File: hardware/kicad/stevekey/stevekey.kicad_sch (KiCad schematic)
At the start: 23 parts, among them J1 ATMEL-ICE-10, J2 Conn_01x04, J3 Conn_01x02, J4 Conn_01x02, J5 Conn_01x02, Q1 2N3904, SW1 SW_SL, SW2 SW_CAPS, SW3 SW_4080, U1 CD4066BM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

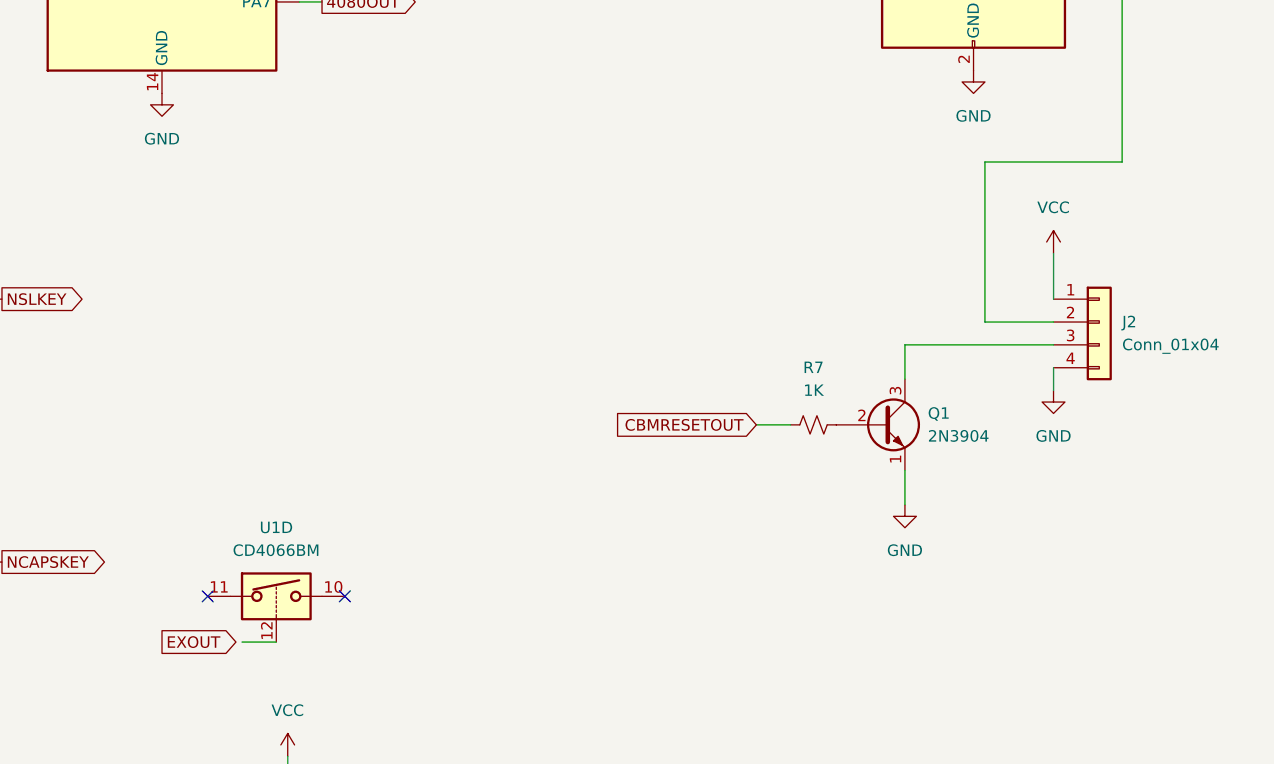
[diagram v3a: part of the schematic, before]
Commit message: Bring the extra 4066 pins out to the header
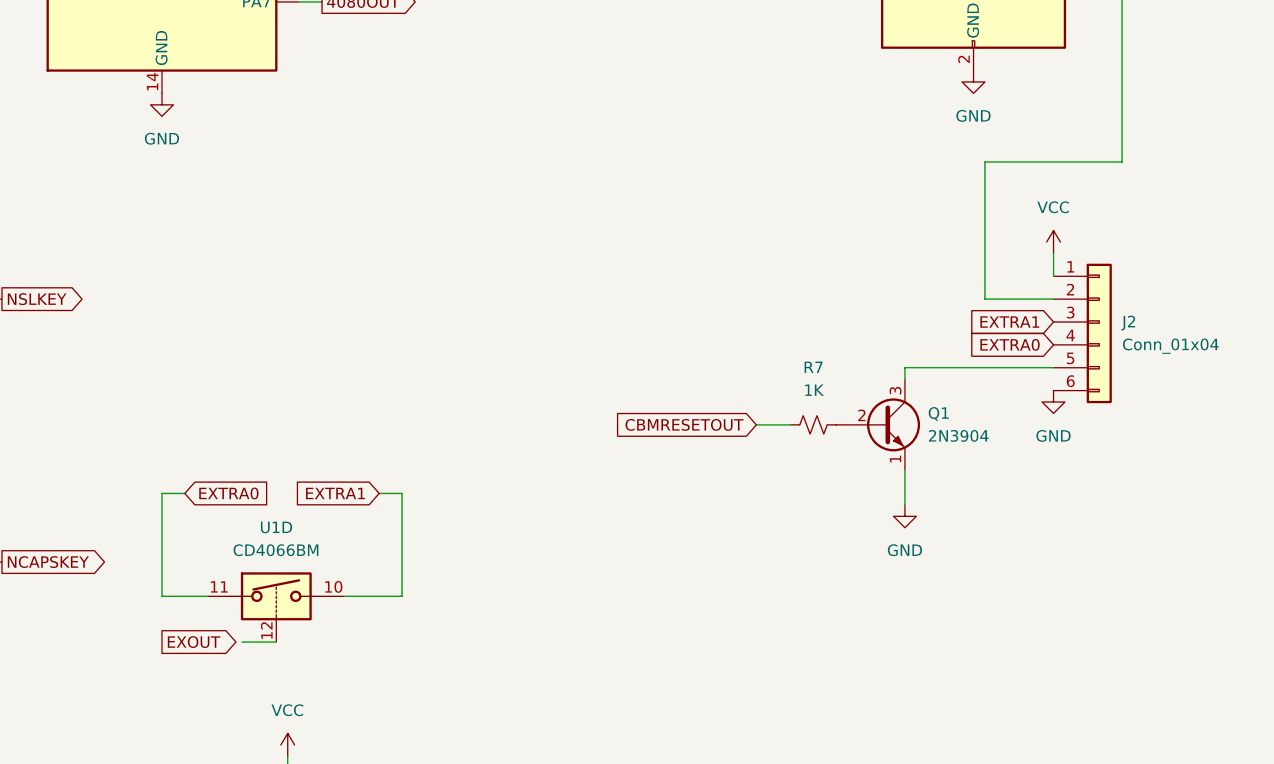
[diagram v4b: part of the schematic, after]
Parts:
- J2: footprint Connector_PinHeader_2.54mm:PinHeader_1x04_P2.54mm_Vertical -> Connector_PinHeader_2.54mm:PinHeader_1x06_P2.54mm_Vertical; symbol Connector_Generic:Conn_01x04 -> Connector_Generic:Conn_01x06
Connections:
- net GND: now also J2.6 (Pin_6); no longer J2.4 (Pin_4)
- net at Q1.3 (C): now also J2.5 (Pin_5); no longer J2.3 (Pin_3)
- net EXTRA1: now reaches U1.10
- net EXTRA1: now also J2.3 (Pin_3)
- net EXTRA0: now reaches U1.11
- net EXTRA0: now also J2.4 (Pin_4)
- no-connect marks 7 -> 5
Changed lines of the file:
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@@
   )
   (no_connect (at 186.69 71.12))
-  (no_connect (at 104.14 147.32))
   (no_connect (at 186.69 66.04))
   (no_connect (at 186.69 73.66))
-  (no_connect (at 88.9 147.32))
   (no_connect (at 186.69 68.58))
   (no_connect (at 186.69 78.74))
@@
     (stroke (width 0) (type default))
   )
+  (wire (pts (xy 107.95 135.89) (xy 110.49 135.89))
+    (stroke (width 0) (type default))
+  )
   (wire (pts (xy 190.5 76.2) (xy 190.5 99.06))
     (stroke (width 0) (type default))
   )
+  (wire (pts (xy 110.49 135.89) (xy 110.49 147.32))
+    (stroke (width 0) (type default))
+  )
   (wire (pts (xy 33.02 116.84) (xy 33.02 105.41))
     (stroke (width 0) (type default))
@@
     (stroke (width 0) (type default))
   )
-  (wire (pts (xy 182.88 121.92) (xy 182.88 124.46))
-    (stroke (width 0) (type default))
-  )
   (wire (pts (xy 40.64 66.04) (xy 53.34 66.04))
     (stroke (width 0) (type default))
@@
     (stroke (width 0) (type default))
   )
+  (wire (pts (xy 182.88 109.22) (xy 182.88 111.76))
+    (stroke (width 0) (type default))
+  )
   (wire (pts (xy 43.18 58.42) (xy 43.18 63.5))
     (stroke (width 0) (type default))
@@
     (stroke (width 0) (type default))
   )
+  (wire (pts (xy 83.82 147.32) (xy 88.9 147.32))
+    (stroke (width 0) (type default))
+  )
   (wire (pts (xy 115.57 55.88) (xy 115.57 58.42))
     (stroke (width 0) (type default))
   )
+  (wire (pts (xy 110.49 147.32) (xy 104.14 147.32))
+    (stroke (width 0) (type default))
+  )
+  (wire (pts (xy 166.37 121.92) (xy 166.37 123.19))
+    (stroke (width 0) (type default))
+  )
   (wire (pts (xy 100.33 59.69) (xy 100.33 63.5))
     (stroke (width 0) (type default))
@@
     (stroke (width 0) (type default))
   )
-  (wire (pts (xy 182.88 109.22) (xy 182.88 114.3))
-    (stroke (width 0) (type default))
-  )
   (wire (pts (xy 53.34 45.72) (xy 53.34 53.34))
     (stroke (width 0) (type default))
@@
     (stroke (width 0) (type default))
   )
-  (wire (pts (xy 175.26 116.84) (xy 175.26 99.06))
+  (wire (pts (xy 175.26 99.06) (xy 175.26 114.3))
     (stroke (width 0) (type default))
   )
@@
     (stroke (width 0) (type default))
   )
-  (wire (pts (xy 182.88 116.84) (xy 175.26 116.84))
-    (stroke (width 0) (type default))
-  )
   (wire (pts (xy 186.69 76.2) (xy 190.5 76.2))
     (stroke (width 0) (type default))
@@
     (stroke (width 0) (type default))
   )
-  (wire (pts (xy 182.88 119.38) (xy 166.37 119.38))
-    (stroke (width 0) (type default))
-  )
   (wire (pts (xy 33.02 167.64) (xy 33.02 179.07))
     (stroke (width 0) (type default))
@@
     (stroke (width 0) (type default))
   )
-  (wire (pts (xy 166.37 119.38) (xy 166.37 123.19))
-    (stroke (width 0) (type default))
-  )
   (wire (pts (xy 99.06 76.2) (xy 101.6 76.2))
     (stroke (width 0) (type default))
@@
     (stroke (width 0) (type default))
   )
+  (wire (pts (xy 83.82 135.89) (xy 83.82 147.32))
+    (stroke (width 0) (type default))
+  )
   (wire (pts (xy 135.89 45.72) (xy 135.89 50.8))
     (stroke (width 0) (type default))
   )
+  (wire (pts (xy 86.36 135.89) (xy 83.82 135.89))
+    (stroke (width 0) (type default))
+  )
   (wire (pts (xy 55.88 114.3) (xy 55.88 118.11))
     (stroke (width 0) (type default))
@@
     (stroke (width 0) (type default))
   )
+  (wire (pts (xy 166.37 121.92) (xy 182.88 121.92))
+    (stroke (width 0) (type default))
+  )
   (wire (pts (xy 99.06 81.28) (xy 101.6 81.28))
     (stroke (width 0) (type default))
@@
     (stroke (width 0) (type default))
   )
+  (wire (pts (xy 182.88 114.3) (xy 175.26 114.3))
+    (stroke (width 0) (type default))
+  )
   (image (at 245.11 80.01) (scale 1.04059)
     (data
@@
     )
   )
+  (global_label "EXTRA1" (shape input) (at 107.95 135.89 180) (fields_autoplaced)
+    (effects (font (size 1.27 1.27)) (justify right))
+    (property "Intersheetrefs" "${INTERSHEET_REFS}" (at 98.0706 135.89 0)
+      (effects (font (size 1.27 1.27)) (justify right) hide)
+    )
+  )
   (global_label "NSLKEY" (shape output) (at 66.04 114.3 0) (fields_autoplaced)
     (effects (font (size 1.27 1.27)) (justify left))
@@
     )
   )
+  (global_label "EXTRA1" (shape input) (at 182.88 116.84 180) (fields_autoplaced)
+    (effects (font (size 1.27 1.27)) (justify right))
+    (property "Intersheetrefs" "${INTERSHEET_REFS}" (at 173.0006 116.84 0)
+      (effects (font (size 1.27 1.27)) (justify right) hide)
+    )
+  )
   (global_label "4080OUT" (shape input) (at 35.56 186.69 180) (fields_autoplaced)
     (effects (font (size 1.27 1.27)) (justify right))
@@
     )
   )
+  (global_label "EXTRA0" (shape input) (at 182.88 119.38 180) (fields_autoplaced)
+    (effects (font (size 1.27 1.27)) (justify right))
+    (property "Intersheetrefs" "${INTERSHEET_REFS}" (at 173.0006 119.38 0)
+      (effects (font (size 1.27 1.27)) (justify right) hide)
+    )
+  )
   (global_label "EXOUT" (shape output) (at 101.6 73.66 0) (fields_autoplaced)
     (effects (font (size 1.27 1.27)) (justify left))
@@
     )
   )
+  (global_label "EXTRA0" (shape input) (at 86.36 135.89 0) (fields_autoplaced)
+    (effects (font (size 1.27 1.27)) (justify left))
+    (property "Intersheetrefs" "${INTERSHEET_REFS}" (at 96.2394 135.89 0)
+      (effects (font (size 1.27 1.27)) (justify left) hide)
+    )
+  )
   (global_label "CBMRESETOUT" (shape input) (at 149.86 128.27 180) (fields_autoplaced)
     (effects (font (size 1.27 1.27)) (justify right))
@@
     )
   )
-  (symbol (lib_id "Connector_Generic:Conn_01x04") (at 187.96 116.84 0) (unit 1)
+  (symbol (lib_id "Connector_Generic:Conn_01x06") (at 187.96 116.84 0) (unit 1)
     (in_bom yes) (on_board yes) (dnp no) (fields_autoplaced)
     (property "Reference" "J2" (at 190.5 116.84 0)
@@
       (effects (font (size 1.27 1.27)) (justify left))
     )
-    (property "Footprint" "Connector_PinHeader_2.54mm:PinHeader_1x04_P2.54mm_Vertical" (at 187.96 116.84 0)
+    (property "Footprint" "Connector_PinHeader_2.54mm:PinHeader_1x06_P2.54mm_Vertical" (at 187.96 116.84 0)
       (effects (font (size 1.27 1.27)) hide)
     )
@@
     (pin "3")
     (pin "4")
+    (pin "5")
+    (pin "6")
     (instances
       (project "stevekey"

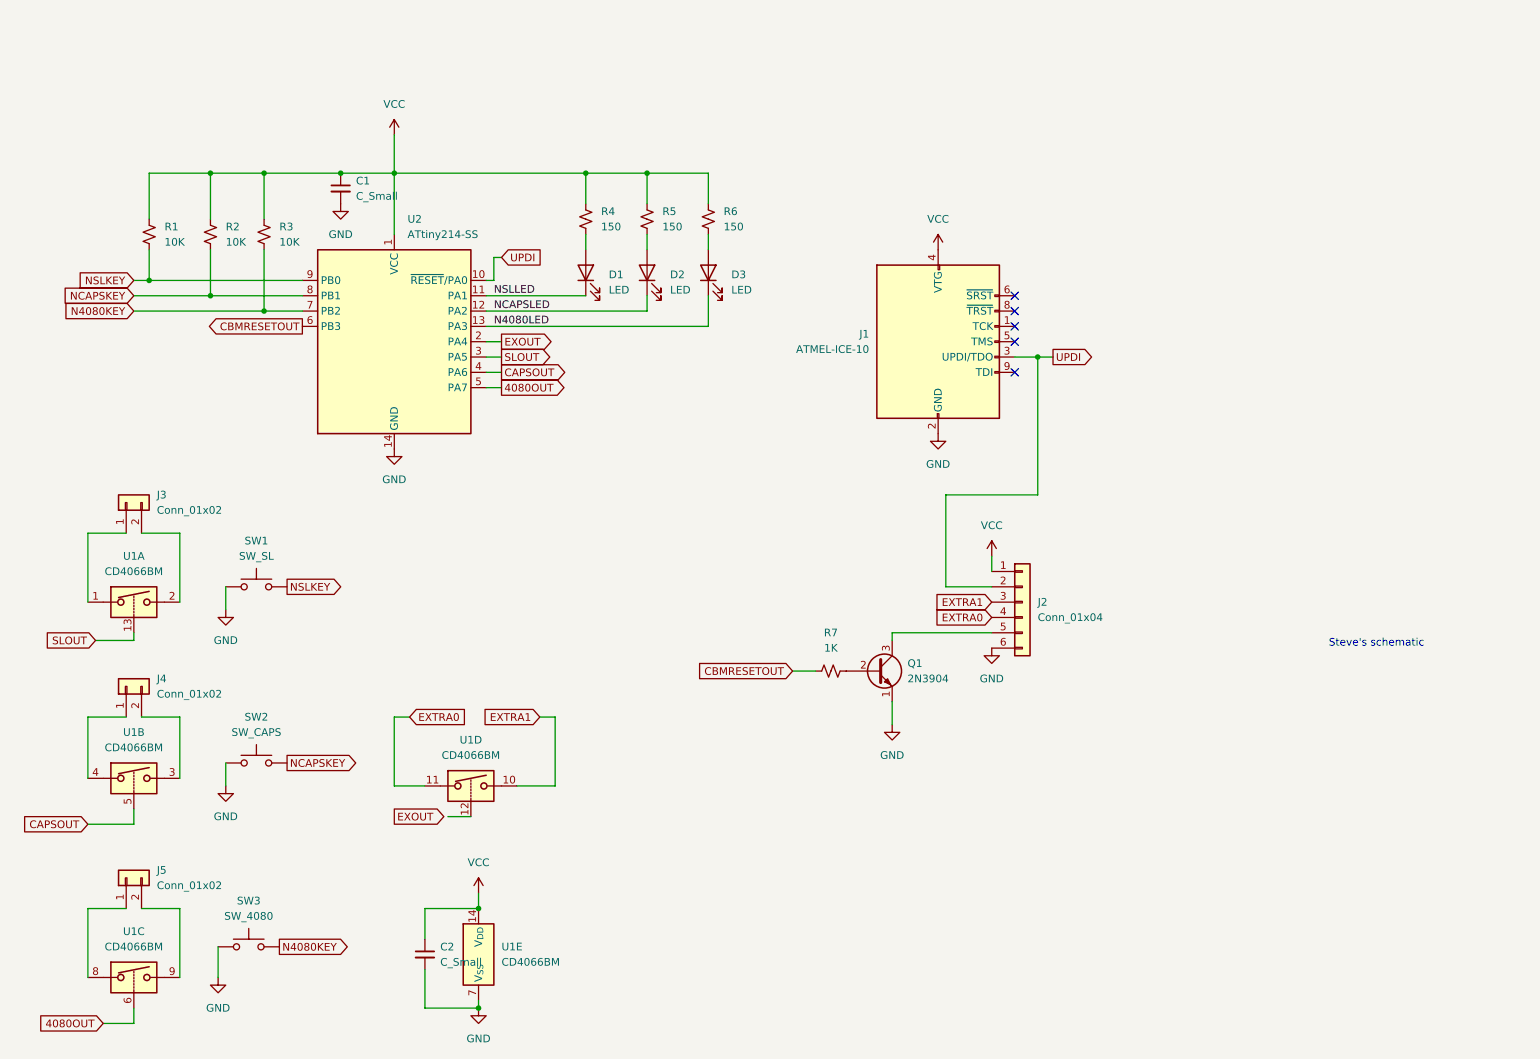
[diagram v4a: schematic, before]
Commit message: Fix values of C1 and C2
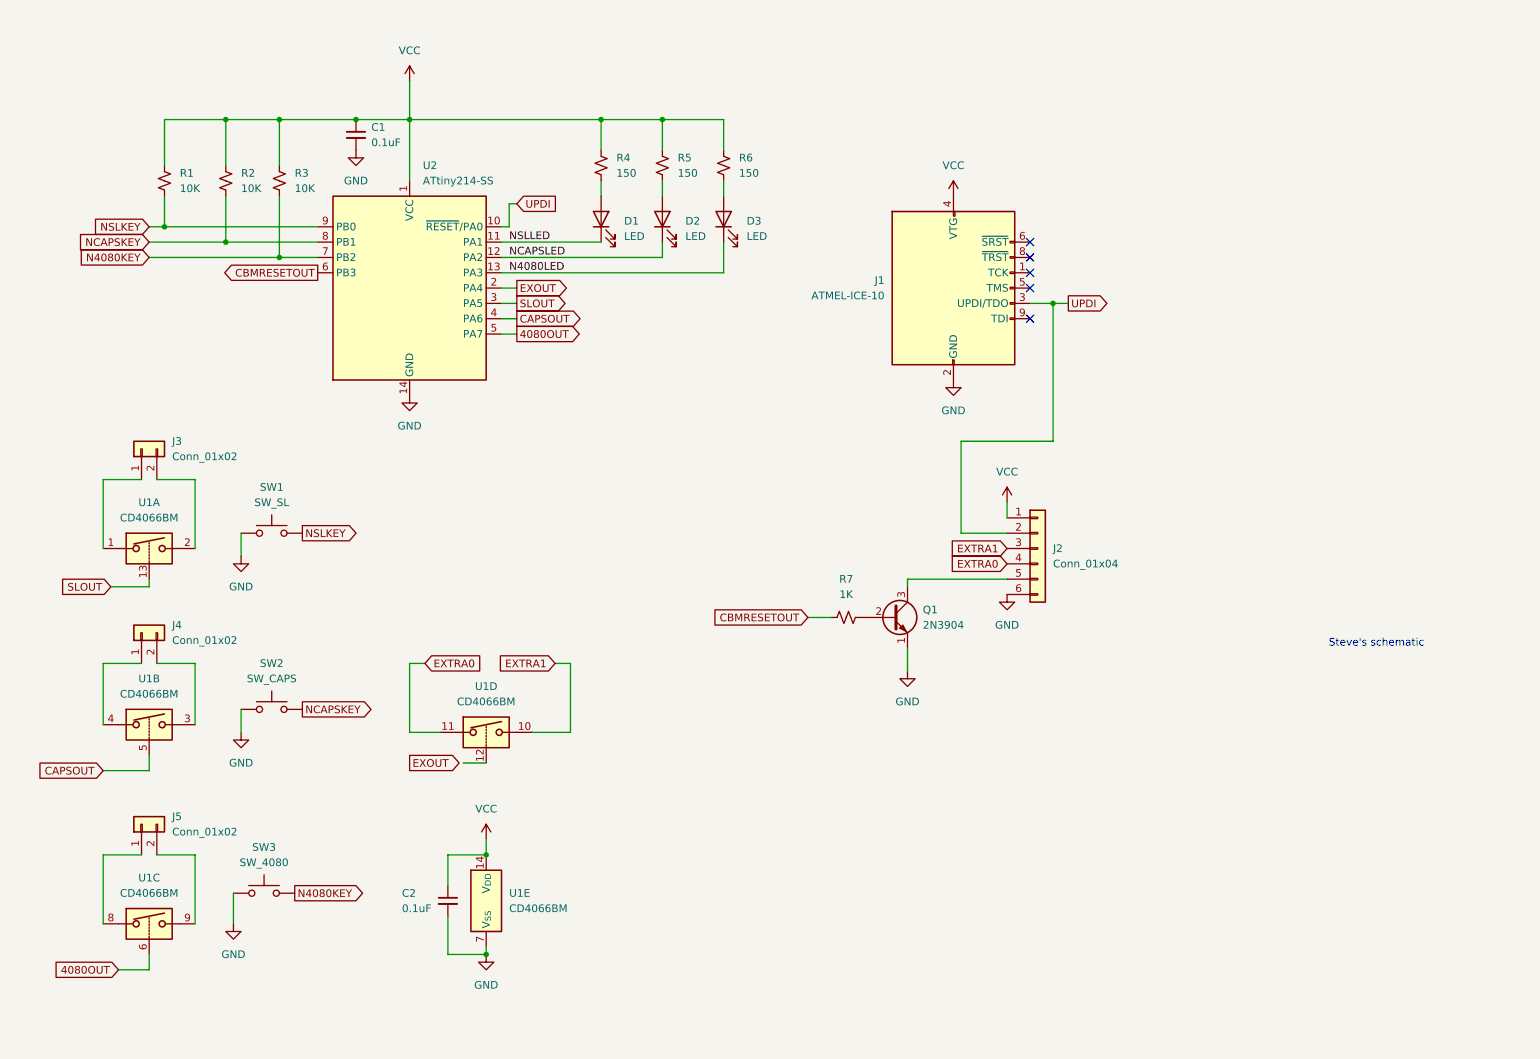
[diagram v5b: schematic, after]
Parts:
- C1, C2: value C_Small -> 0.1uF
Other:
- moved on the sheet: C1, C2, D1, D2, D3, J1, J2, J3, J4, J5, Q1, R1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

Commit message: Add capacitor on input power
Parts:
- added C3: 10uF, Capacitor_THT:CP_Radial_D6.3mm_P2.50mm, symbol Device:C_Polarized_Small
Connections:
- net EXOUT: now also U1.12
- net GND: now also C3.2
- net VCC: now also C3.1
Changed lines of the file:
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@@
   (junction (at 86.36 36.83) (diameter 0) (color 0 0 0 0)
   )
+  (junction (at 185.42 102.87) (diameter 0) (color 0 0 0 0)
+  )
   (junction (at 55.88 57.15) (diameter 0) (color 0 0 0 0)
   )
@@
   (junction (at 118.11 36.83) (diameter 0) (color 0 0 0 0)
   )
+  (junction (at 185.42 115.57) (diameter 0) (color 0 0 0 0)
+  )
   (junction (at 64.77 36.83) (diameter 0) (color 0 0 0 0)
   )
@@
     (stroke (width 0) (type default))
   )
+  (wire (pts (xy 185.42 115.57) (xy 196.85 115.57))
+    (stroke (width 0) (type default))
+  )
   (wire (pts (xy 193.04 67.31) (xy 193.04 90.17))
     (stroke (width 0) (type default))
@@
     (stroke (width 0) (type default))
   )
+  (wire (pts (xy 185.42 100.33) (xy 185.42 102.87))
+    (stroke (width 0) (type default))
+  )
   (wire (pts (xy 35.56 107.95) (xy 35.56 96.52))
     (stroke (width 0) (type default))
@@
     (stroke (width 0) (type default))
   )
+  (wire (pts (xy 196.85 102.87) (xy 196.85 106.68))
+    (stroke (width 0) (type default))
+  )
   (wire (pts (xy 50.8 158.75) (xy 50.8 170.18))
     (stroke (width 0) (type default))
@@
     (stroke (width 0) (type default))
   )
-  (wire (pts (xy 185.42 100.33) (xy 185.42 102.87))
-    (stroke (width 0) (type default))
-  )
   (wire (pts (xy 45.72 49.53) (xy 45.72 54.61))
     (stroke (width 0) (type default))
@@
     (stroke (width 0) (type default))
   )
+  (wire (pts (xy 185.42 102.87) (xy 196.85 102.87))
+    (stroke (width 0) (type default))
+  )
   (wire (pts (xy 43.18 114.3) (xy 36.83 114.3))
     (stroke (width 0) (type default))
@@
     (stroke (width 0) (type default))
   )
+  (wire (pts (xy 196.85 115.57) (xy 196.85 111.76))
+    (stroke (width 0) (type default))
+  )
   (wire (pts (xy 101.6 64.77) (xy 104.14 64.77))
     (stroke (width 0) (type default))
@@
     )
   )
-  (global_label "EXOUT" (shape output) (at 86.36 143.51 0) (fields_autoplaced)
-    (effects (font (size 1.27 1.27)) (justify left))
-    (property "Intersheetrefs" "${INTERSHEET_REFS}" (at 95.3323 143.51 0)
-      (effects (font (size 1.27 1.27)) (justify left) hide)
+  (global_label "EXOUT" (shape input) (at 95.25 143.51 180) (fields_autoplaced)
+    (effects (font (size 1.27 1.27)) (justify right))
+    (property "Intersheetrefs" "${INTERSHEET_REFS}" (at 86.2777 143.51 0)
+      (effects (font (size 1.27 1.27)) (justify right) hide)
     )
   )
@@
   )
   (symbol (lib_id "Device:R_Small_US") (at 158.75 119.38 90) (unit 1)
-    (in_bom yes) (on_board yes) (dnp no) (fields_autoplaced)
-    (property "Reference" "R7" (at 158.75 113.03 90)
+    (in_bom yes) (on_board yes) (dnp no)
+    (property "Reference" "R7" (at 158.75 123.19 90)
       (effects (font (size 1.27 1.27)))
     )
-    (property "Value" "1K" (at 158.75 115.57 90)
+    (property "Value" "1K" (at 158.75 125.73 90)
       (effects (font (size 1.27 1.27)))
     )
@@
     )
   )
+  (symbol (lib_id "Device:C_Polarized_Small") (at 196.85 109.22 0) (unit 1)
+    (in_bom yes) (on_board yes) (dnp no)
+    (property "Reference" "C3" (at 199.39 107.95 0)
+      (effects (font (size 1.27 1.27)) (justify left))
+    )
+    (property "Value" "10uF" (at 199.39 110.49 0)
+      (effects (font (size 1.27 1.27)) (justify left))
+    )
+    (property "Footprint" "Capacitor_THT:CP_Radial_D6.3mm_P2.50mm" (at 196.85 109.22 0)
+      (effects (font (size 1.27 1.27)) hide)
+    )
+    (property "Datasheet" "~" (at 196.85 109.22 0)
+      (effects (font (size 1.27 1.27)) hide)
+    )
+    (pin "1")
+    (pin "2")
+    (instances
+      (project "stevekey"
+        (path "/4393a5c5-44f8-4de9-9c92-ea247f2f7df2"
+          (reference "C3") (unit 1)
+        )
+      )
+    )
+  )
   (symbol (lib_id "power:GND") (at 57.15 170.18 0) (unit 1)
     (in_bom yes) (on_board yes) (dnp no) (fields_autoplaced)
@@
   )
   (symbol (lib_id "Connector_Generic:Conn_01x06") (at 190.5 107.95 0) (unit 1)
-    (in_bom yes) (on_board yes) (dnp no) (fields_autoplaced)
-    (property "Reference" "J2" (at 193.04 107.95 0)
+    (in_bom yes) (on_board yes) (dnp no)
+    (property "Reference" "J2" (at 189.23 123.19 0)
       (effects (font (size 1.27 1.27)) (justify left))
     )
-    (property "Value" "Conn_01x04" (at 193.04 110.49 0)
+    (property "Value" "Conn_01x04" (at 184.15 125.73 0)
       (effects (font (size 1.27 1.27)) (justify left))
     )
